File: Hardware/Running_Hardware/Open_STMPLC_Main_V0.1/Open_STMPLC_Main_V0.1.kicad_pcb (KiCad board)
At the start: 4 copper layers, 168.8 x 90 mm, 184 parts, among them J1 Conn_02x08_Odd_Even, J10 10144518-041802LF, J12 USB C, J13 RJ45_Hanrun_HR911105A_Horizon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, J2 USB C, J3 Conn_01x04, J4 TF-01A, J5 Conn_Coaxial, J6 Conn_Coaxial, J7 Simcard_Nano, J8 10144518-041802LF, J9 10144518-041802LF, Q1 DTC143Z, Q2 DTC143Z, Q3 DTC143Z, Q4 DTC143Z, Q5 DTC143Z, Q6 DTC143Z, Q7 DTC143Z, Q8 DTC143Z, SW1 Switch_6x6, SW2 SW_DIP_x01, SW3 Switch_6x6, U1 STM32F407IGTx, U10 AP63205WU, U2 ADM2587E, U3 TPS3430WDRC, U4 CH340C, U5 AMS1117-3.3, U6 W25Q64JVSSIQ, U7 LAN8720A, U8 EC200U, U9 AP63200WU, Y1 48MHz, Y2 32.768kHz, Y3 25MHz

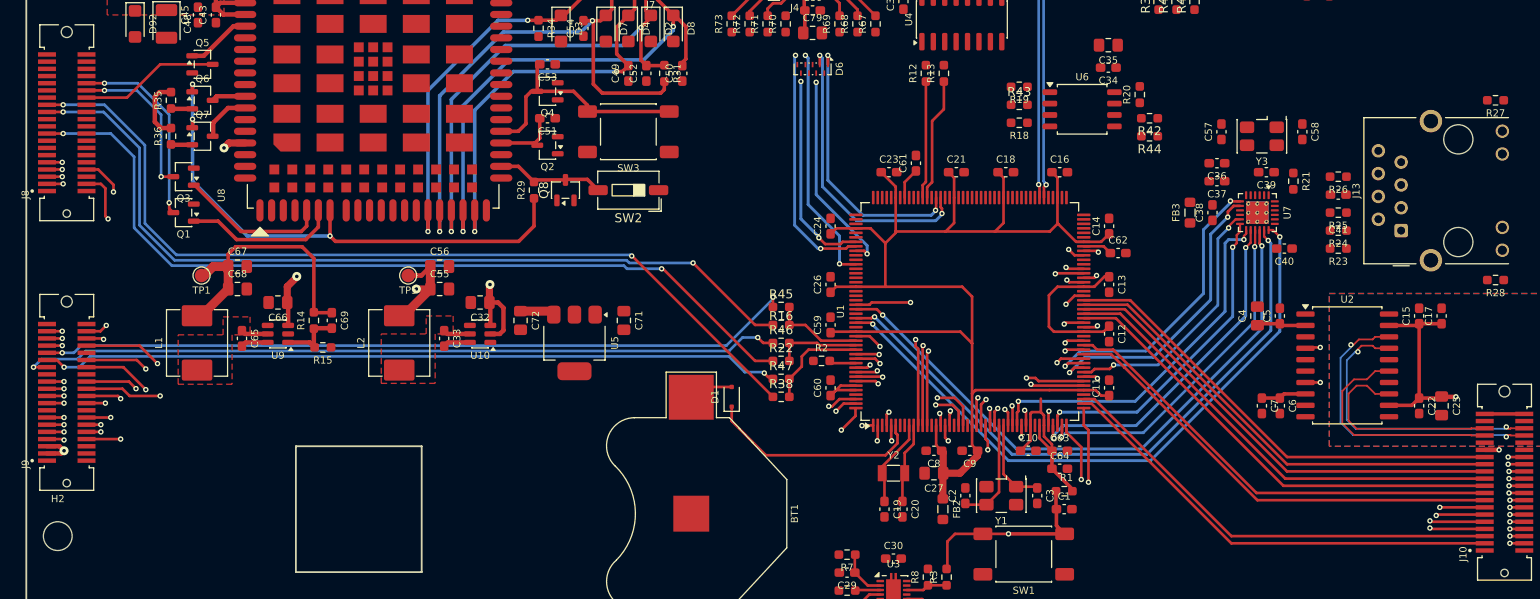
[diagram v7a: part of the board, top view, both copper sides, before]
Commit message: MCU Pin mapping
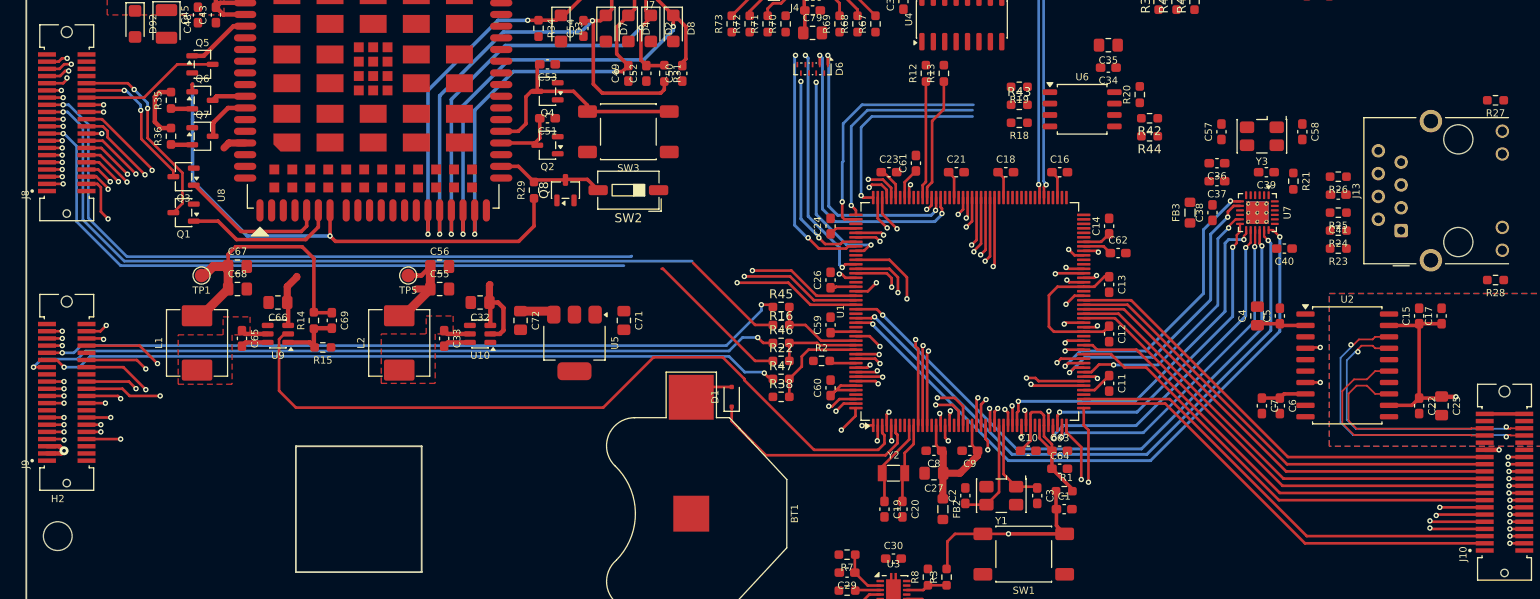
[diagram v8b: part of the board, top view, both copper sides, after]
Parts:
- moved C11 0.50 mm to (170.5, 109.0), turned to -90 degrees
- moved C26 0.50 mm to (139.5, 97.5)
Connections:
- U1 pad 105: unconnected-(U1-PD15-Pad105) -> /B2B_Connector/THRM_~{FAULT}
- U1 pad 106: unconnected-(U1-PG2-Pad106) -> /B2B_Connector/RTD_~{DRDY}_1
- U1 pad 107: unconnected-(U1-PG3-Pad107) -> /B2B_Connector/AOUT_EFOT_1
- U1 pad 108: unconnected-(U1-PG4-Pad108) -> /B2B_Connector/AOUT_EFLD_1
- U1 pad 109: unconnected-(U1-PG5-Pad109) -> /B2B_Connector/AOUT_EFCM_1
- U1 pad 110: unconnected-(U1-PG6-Pad110) -> /B2B_Connector/DIG_IN_1
- U1 pad 111: unconnected-(U1-PG7-Pad111) -> /B2B_Connector/DIG_IN_2
- U1 pad 112: unconnected-(U1-PG8-Pad112) -> /B2B_Connector/DIG_IN_3
- U1 pad 119: unconnected-(U1-PA8-Pad119) -> /B2B_Connector/DIG_IN_4
- U1 pad 124: unconnected-(U1-PA13-Pad124) -> /B2B_Connector/DIG_IN_5
- U1 pad 128: unconnected-(U1-PH13-Pad128) -> /B2B_Connector/DIG_IN_6
- U1 pad 129: unconnected-(U1-PH14-Pad129) -> /B2B_Connector/RTD_~{DRDY}_2
- U1 pad 130: unconnected-(U1-PH15-Pad130) -> /B2B_Connector/THRM_~{DRDY}
- U1 pad 131: unconnected-(U1-PI0-Pad131) -> /B2B_Connector/RTD_~{CS}_2
- U1 pad 137: unconnected-(U1-PA14-Pad137) -> /B2B_Connector/RTD_~{CS}_1
- U1 pad 138: unconnected-(U1-PA15-Pad138) -> /B2B_Connector/THRM_~{CS}
- U1 pad 143: unconnected-(U1-PD1-Pad143) -> /B2B_Connector/AOUT_M1_2
- U1 pad 145: unconnected-(U1-PD3-Pad145) -> /B2B_Connector/AOUT_M2_2
- U1 pad 146: unconnected-(U1-PD4-Pad146) -> /B2B_Connector/AOUT_~{OD}_2
- U1 pad 151: unconnected-(U1-PD7-Pad151) -> /B2B_Connector/AOUT_EFCM_2
- U1 pad 152: unconnected-(U1-PG9-Pad152) -> /B2B_Connector/AOUT_EFLD_2
- U1 pad 153: /B2B_Connector/AOUT_M2_2 -> /B2B_Connector/AOUT_EFOT_2
- U1 pad 3: unconnected-(U1-PE4-Pad3) -> /B2B_Connector/3V8_EN
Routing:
- net /B2B_Connector/THRM_~{FAULT}: track 0.00 -> 117.3 mm, vias 0 -> 2
- net /B2B_Connector/DIG_IN_1: track 0.00 -> 117.2 mm, vias 0 -> 2
- net /B2B_Connector/RTD_~{DRDY}_1: track 0.00 -> 115.6 mm, vias 0 -> 2
- net /B2B_Connector/AOUT_EFOT_1: track 0.00 -> 115.6 mm, vias 0 -> 2
- net /B2B_Connector/AOUT_EFLD_1: track 0.00 -> 114.7 mm, vias 0 -> 2
- net /B2B_Connector/AOUT_EFCM_1: track 0.00 -> 113.8 mm, vias 0 -> 2
- net /B2B_Connector/DIG_IN_2: track 0.00 -> 113.7 mm, vias 0 -> 2
- net /B2B_Connector/DIG_IN_3: track 0.00 -> 111.6 mm, vias 0 -> 2
- net /B2B_Connector/DIG_IN_4: track 0.00 -> 107.4 mm, vias 0 -> 2
- net /B2B_Connector/AOUT_M1_2: track 0.00 -> 105.9 mm, vias 0 -> 2
- net /Microcontroller/3V3_MCU: track 191.9 -> 89.2 mm
- net /B2B_Connector/DIG_IN_5: track 0.00 -> 102.6 mm, vias 0 -> 2
- net /B2B_Connector/RTD_~{CS}_2: track 0.00 -> 102.3 mm, vias 0 -> 2
- net /B2B_Connector/RTD_~{CS}_1: track 0.00 -> 101.3 mm, vias 0 -> 2
- net /B2B_Connector/AOUT_~{OD}_2: track 0.00 -> 100.7 mm, vias 0 -> 2
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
